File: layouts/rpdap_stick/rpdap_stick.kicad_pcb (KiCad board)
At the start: 4 copper layers, 66 x 43.2 mm, 67 parts

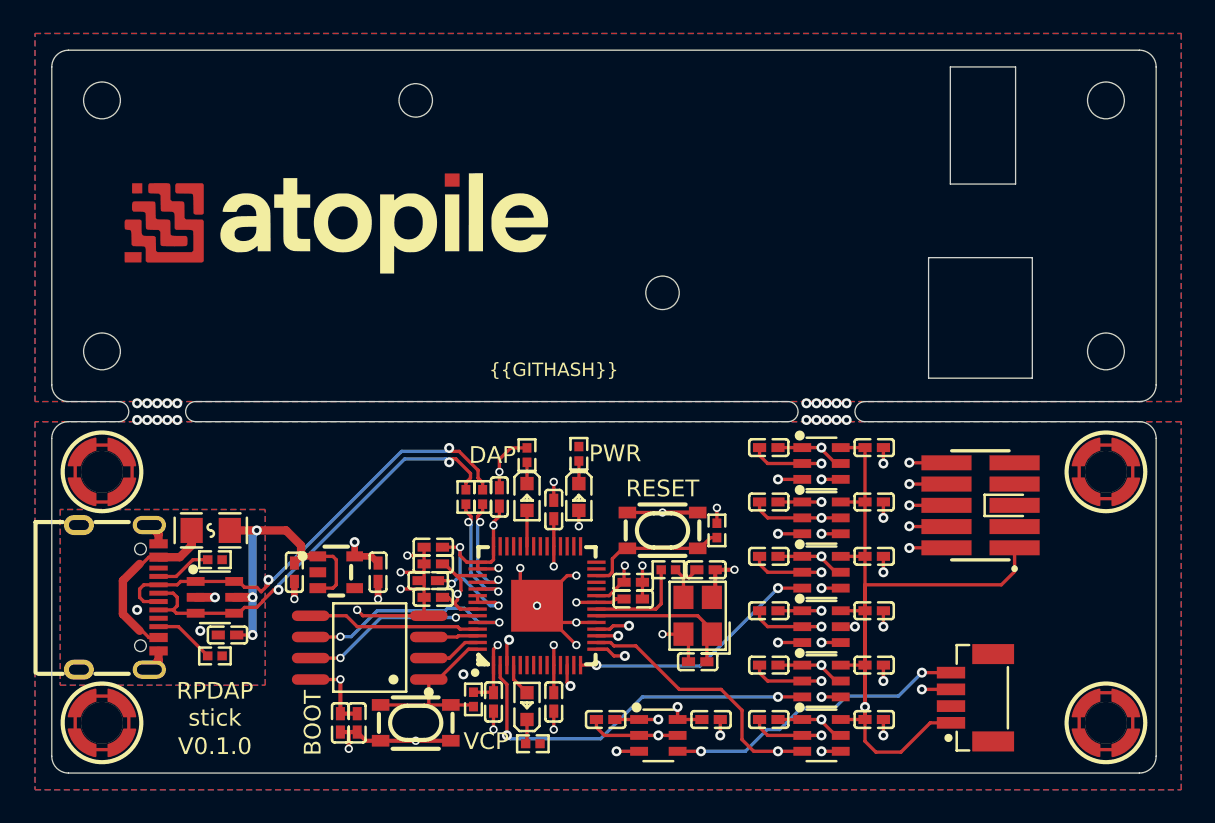
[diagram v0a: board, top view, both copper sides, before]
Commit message: fix swapped jlink connector pinout + update deps
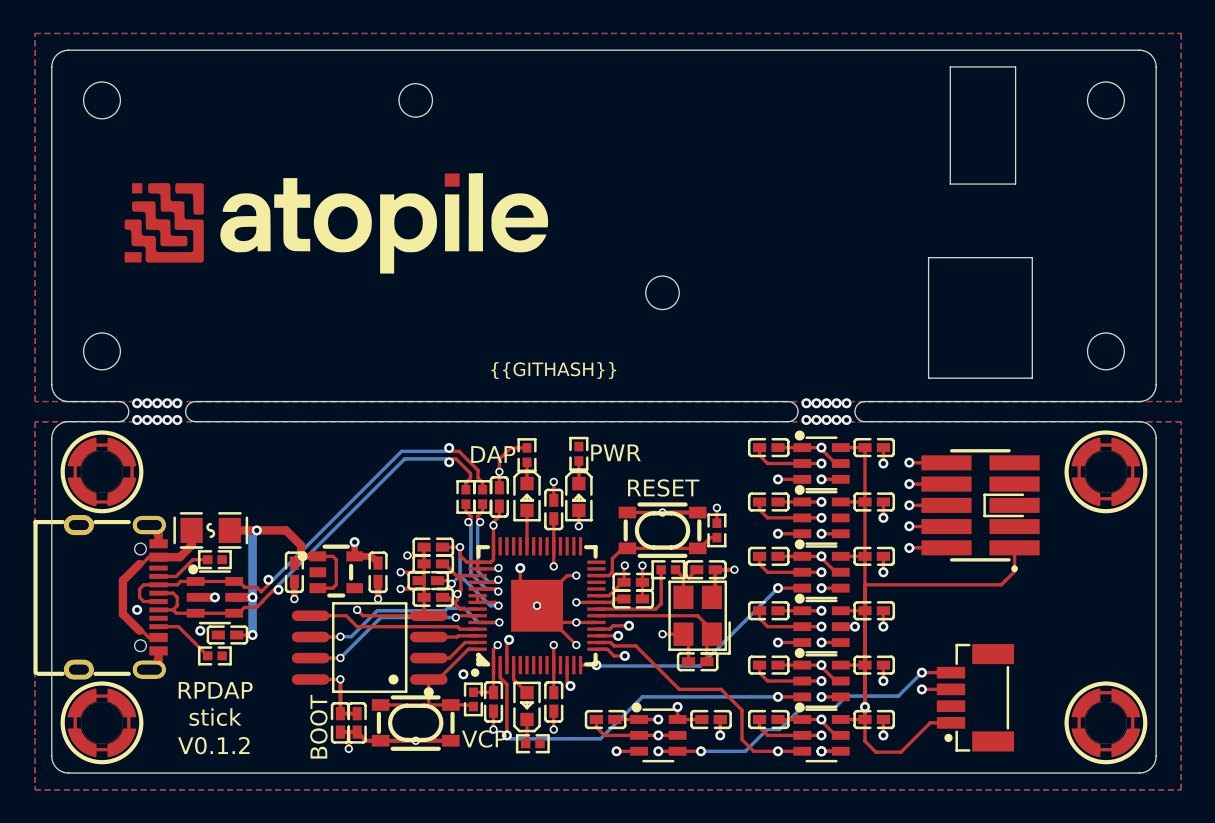
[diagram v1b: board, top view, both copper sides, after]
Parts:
- removed C32, C33: 100nF ±10% 16V X7R, Samsung_Electro_Mechanics_CL05B104KO5NNNC:C0402
- removed R13, R14: 5.1kΩ ±1% 62.5mW, UNI_ROYAL_0402WGF5101TCE:R0402
- added C15: 100nF ±10% 16V X7R, Samsung_Electro_Mechanics_CL05B104KO5NNNC:C0402, F.Cu at (33.1, 18.4)
- added C30: 100nF ±10% 16V X7R, Samsung_Electro_Mechanics_CL05B104KO5NNNC:C0402, F.Cu at (18.2, 18.6)
- added R10: 5.1kΩ ±1% 62.5mW, UNI_ROYAL_0402WGF5101TCE:R0402, F.Cu at (9.75, 14.6)
- added R9: 5.1kΩ ±1% 62.5mW, UNI_ROYAL_0402WGF5101TCE:R0402, F.Cu at (9.75, 8.85)
- C16, C28: value 2.2µF ±20% 6.3V X5R -> 100nF ±10% 16V X7R; footprint Samsung_Electro_Mechanics_CL05A225MQ5NSNC:C0402 -> Samsung_Electro_Mechanics_CL05B104KO5NNNC:C0402
- C17, C22, C29: value 100nF ±10% 16V X7R -> 2.2µF ±10% 16V X5R; footprint Samsung_Electro_Mechanics_CL05B104KO5NNNC:C0402 -> Samsung_Electro_Mechanics_CL05A225KO5NQNC:C0402
- C19: value 15pF ±5% 50V C0G -> 100nF ±10% 16V X7R; footprint FH_0402CG150J500NT:C0402 -> Samsung_Electro_Mechanics_CL05B104KO5NNNC:C0402
- C21: value 2.2µF ±20% 6.3V X5R -> 15pF ±5% 50V C0G; footprint Samsung_Electro_Mechanics_CL05A225MQ5NSNC:C0402 -> FH_0402CG150J500NT:C0402
- R1, R3: value 1kΩ ±1% 62.5mW -> 10kΩ ±1% 62.5mW; footprint UNI_ROYAL_0402WGF1001TCE:R0402 -> UNI_ROYAL_0402WGF1002TCE:R0402
- R2: value 10kΩ ±1% 62.5mW -> 1kΩ ±1% 62.5mW; footprint UNI_ROYAL_0402WGF1002TCE:R0402 -> UNI_ROYAL_0402WGF1001TCE:R0402
- R5: value 10kΩ ±1% 62.5mW -> 27Ω ±1% 62.5mW; footprint UNI_ROYAL_0402WGF1002TCE:R0402 -> UNI_ROYAL_0402WGF270JTCE:R0402
- R6: footprint YAGEO_RC0402FR_0727RL:R0402 -> UNI_ROYAL_0402WGF270JTCE:R0402
- R7: value 27Ω ±1% 62.5mW -> 1kΩ ±1% 62.5mW; footprint YAGEO_RC0402FR_0727RL:R0402 -> UNI_ROYAL_0402WGF1001TCE:R0402
- moved C16 19.0 mm to (39.4, 18.4), turned to 0 degrees
- moved C21 16.4 mm to (39.1, 9.45), turned to 0 degrees
- moved R1 16.0 mm to (25.2, 17.2)
- moved R5 15.1 mm to (24.8, 5.10), turned to -90 degrees
- moved R2 14.0 mm to (36.9, 9.45), turned to 180 degrees
- moved C28 12.8 mm to (30.0, 17.4)
- moved C23 12.3 mm to (22.5, 10.1), turned to 180 degrees
- moved R4 12.2 mm to (39.8, 7.10), turned to 90 degrees
- moved C26 12.1 mm to (30.0, 5.85), turned to 90 degrees
- moved C18 12.0 mm to (22.8, 11.1), turned to 180 degrees
- moved R3 10.9 mm to (28.4, 2.60), turned to -90 degrees
- moved C24 10.1 mm to (34.8, 11.2), turned to 0 degrees
- moved R7 6.30 mm to (31.5, 2.52), turned to 90 degrees
- moved C19 6.11 mm to (34.8, 10.2), turned to 0 degrees
- moved C20 5.52 mm to (38.6, 14.9), turned to 180 degrees
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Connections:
- net A renamed input-A
- net _power_vbus-VCC renamed Vbus_fused
- net a-RX renamed mcu-uart-RX
- net a-TX renamed mcu-uart-TX
- net dir-line renamed DIR
- net model-a-line-0 renamed gpio[12]-A
- net model-a-line-1 renamed gpio[11]-A
- net model-a-line-2 renamed gpio[14]-A
- net model-a-line-3 renamed gpio[15]-A
- net model-a-line-4 renamed gpio[13]-A
- net power-anode renamed anode
- net uart-RX renamed uart_connector-uart-RX
- net uart-TX renamed uart_connector-uart-TX
- C11 pad 1: _power_3v3-anode -> 3V3
- C13 pad 1: _power_3v3-anode -> 3V3
- C16 pad 1: _core_regulator_out_power-VCC -> reference-VCC
- C19 pad 1: XIN -> _core_regulator_out_power-VCC
- C2 pad 1: _power_3v3-anode -> 3V3
- C20 pad 1: output -> XIN
- C21 pad 1: _power_3v3-anode -> output
- C22 pad 1: _power_3v3-anode -> 3V3
- C23 pad 1: _power_3v3-anode -> 3V3
- C24 pad 1: _power_3v3-anode -> 3V3
- C25 pad 1: _power_3v3-anode -> 3V3
- C26 pad 1: _power_3v3-anode -> 3V3
- C27 pad 1: _power_3v3-anode -> 3V3
- C28 pad 1: _power_3v3-anode -> 3V3
- C29 pad 1: _power_3v3-anode -> 3V3
- C3 pad 1: _power_3v3-anode -> 3V3
- C5 pad 1: _power_3v3-anode -> 3V3
- C7 pad 1: _power_3v3-anode -> 3V3
- C9 pad 1: _power_3v3-anode -> 3V3
- LED2 pad 2: _power_3v3-anode -> 3V3
- R1 pad 1: footprint-cathode-0 -> chip_select
- R1 pad 2: GND -> 3V3
- R2 pad 1: chip_select -> output
- R2 pad 2: _power_3v3-anode -> XOUT
- R3 pad 1: output -> GND
- R3 pad 2: XOUT -> K
- R4 pad 1: GND -> RUN
- R4 pad 2: K -> 3V3
- R5 pad 1: RUN -> input-USB_D_P
- R5 pad 2: _power_3v3-anode -> output-USB_D_P
- R6 pad 1: input-USB_D_P -> input-USB_D_N
- R6 pad 2: output-USB_D_P -> output-USB_D_N
- R7 pad 1: input-USB_D_N -> footprint-cathode-0
- R7 pad 2: output-USB_D_N -> GND
- U1 pad 5: _power_3v3-anode -> 3V3
- U15 pad 1: _power_3v3-anode -> 3V3
- U2 pad 1: _power_3v3-anode -> 3V3
- U3 pad 1: _power_3v3-anode -> 3V3
- U3 pad 5: _power_3v3-anode -> 3V3
- U4 pad 1: _power_3v3-anode -> 3V3
- U5 pad 1: _power_3v3-anode -> 3V3
- U5 pad 5: _power_3v3-anode -> 3V3
- U6 pad 1: _power_3v3-anode -> 3V3
- U6 pad 5: _power_3v3-anode -> 3V3
- U7 pad 1: _power_3v3-anode -> 3V3
- U7 pad 5: _power_3v3-anode -> 3V3
- U8 pad 1: _power_3v3-anode -> 3V3
- U8 pad 10: _power_3v3-anode -> 3V3
- U8 pad 22: _power_3v3-anode -> 3V3
- U8 pad 33: _power_3v3-anode -> 3V3
- U8 pad 42: _power_3v3-anode -> 3V3
- U8 pad 43: _power_3v3-anode -> 3V3
- U8 pad 44: _power_3v3-anode -> 3V3
- U8 pad 48: _power_3v3-anode -> 3V3
- U8 pad 49: _power_3v3-anode -> 3V3
- U9 pad 8: _power_3v3-anode -> 3V3
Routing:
- net (no net): track 141.7 -> 0.00 mm, vias 59 -> 21
- net GND: track 0.00 -> 140.6 mm, vias 0 -> 38
- net _power_3v3-anode: track 63.9 -> 0.00 mm, vias 20 -> 0
- net 3V3: track 0.00 -> 63.9 mm, vias 0 -> 20
- net uart_connector-uart-RX: track 18.3 -> 19.4 mm, vias 2 -> 3
- net TDI: track 28.0 -> 29.2 mm, vias 2 -> 3
- added copper zone on In1.Cu, net (none)
- added copper zone on In1.Cu, net 3V3
- added copper zone on B.Cu, net GND
- added copper zone on F.Cu, net GND
- added copper zone on In2.Cu, net GND
- removed copper zone on In1.Cu, net _power_3v3-anode
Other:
- board text added: "V0.1.2"
- board text removed: "V0.1.0"
- board text removed: "V0.1.1"
